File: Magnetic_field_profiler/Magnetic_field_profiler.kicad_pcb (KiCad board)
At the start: 4 copper layers, 130 x 100 mm, 91 parts, among them J1 USB_B_Micro, J2 Conn_01x04_Socket, J3 Conn_01x04_Socket, J4 Screw_Terminal_01x06, Q1 BSS123, SW1 SW_SPDT, U1 STM32F103C8Tx, U10 MLX90393, U11 MLX90393, U12 MLX90393, U13 TP6841S6, U2 MLX90393, U3 DRV8825, U4 DRV8825, U5 MLX90393, U6 MLX90393, U7 MLX90393, U8 MLX90393, U9 MLX90393, Y1 Crystal_GND24

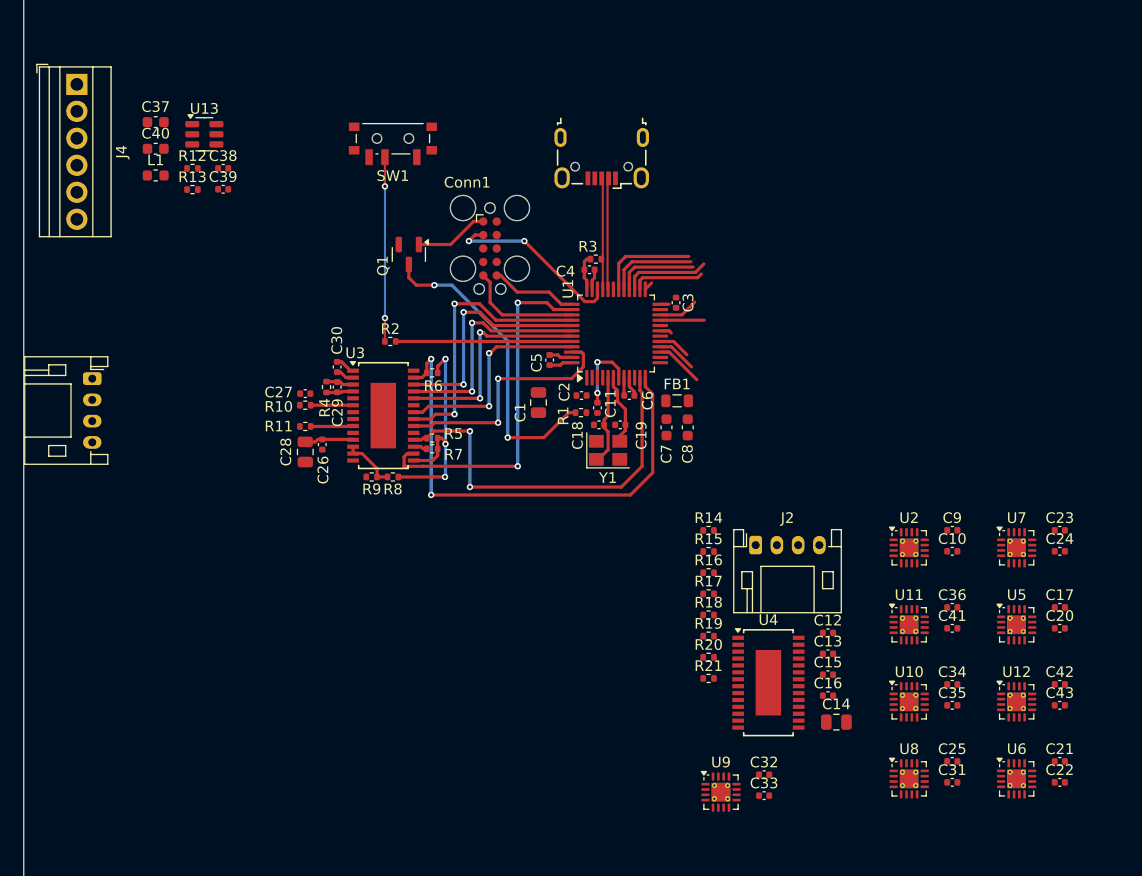
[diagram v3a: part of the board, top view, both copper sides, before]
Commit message: IO expander connections complete and PCB layout restarted
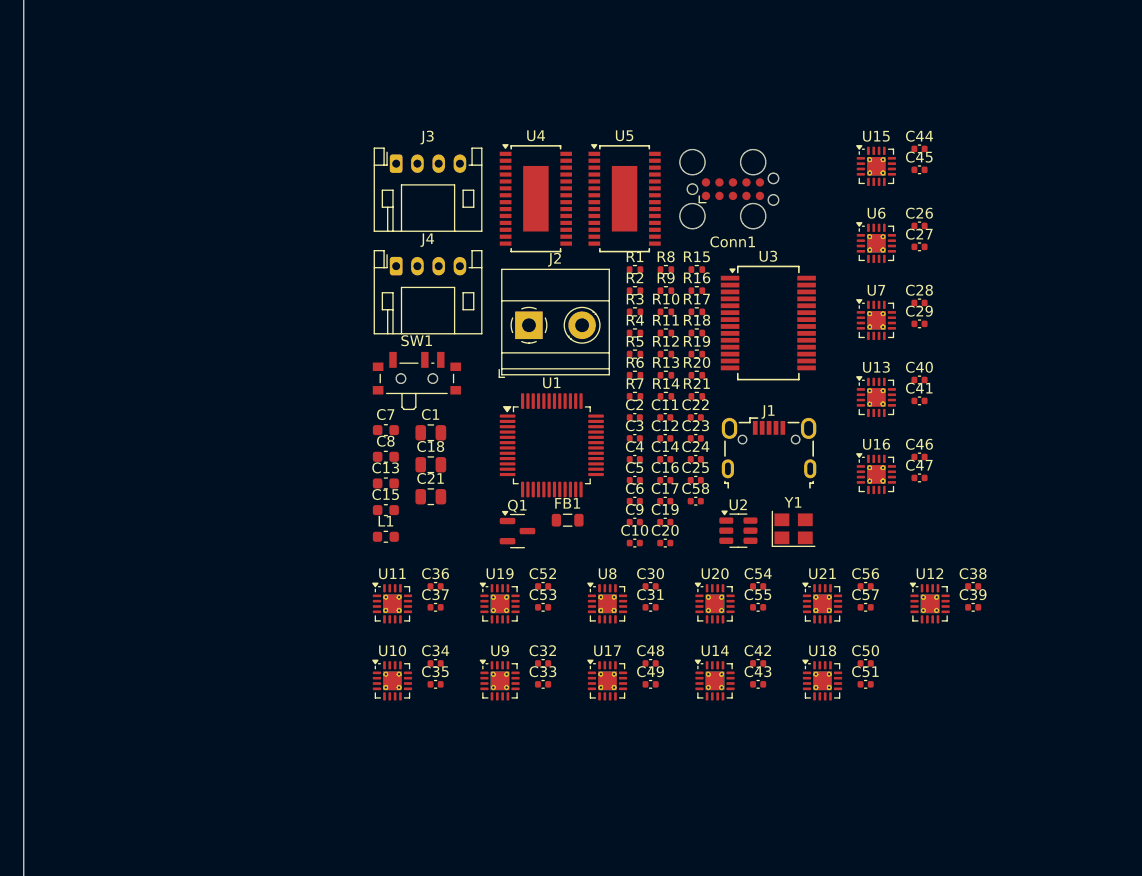
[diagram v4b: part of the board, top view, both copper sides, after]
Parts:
- added C44: 100n, Capacitor_SMD:C_0402_1005Metric, F.Cu at (139.3, 76.4)
- added C45: 100n, Capacitor_SMD:C_0402_1005Metric, F.Cu at (139.3, 78.3)
- added C46: 100n, Capacitor_SMD:C_0402_1005Metric, F.Cu at (139.3, 105.4)
- added C47: 100n, Capacitor_SMD:C_0402_1005Metric, F.Cu at (139.3, 107.3)
- added C48: 100n, Capacitor_SMD:C_0402_1005Metric, F.Cu at (114.0, 124.8)
- added C49: 100n, Capacitor_SMD:C_0402_1005Metric, F.Cu at (114.0, 126.8)
- added C50: 100n, Capacitor_SMD:C_0402_1005Metric, F.Cu at (134.2, 124.8)
- added C51: 100n, Capacitor_SMD:C_0402_1005Metric, F.Cu at (134.2, 126.8)
- added C52: 100n, Capacitor_SMD:C_0402_1005Metric, F.Cu at (103.9, 117.6)
- added C53: 100n, Capacitor_SMD:C_0402_1005Metric, F.Cu at (103.9, 119.5)
- added C54: 100n, Capacitor_SMD:C_0402_1005Metric, F.Cu at (124.1, 117.6)
- added C55: 100n, Capacitor_SMD:C_0402_1005Metric, F.Cu at (124.1, 119.5)
- added C56: 100n, Capacitor_SMD:C_0402_1005Metric, F.Cu at (134.2, 117.6)
- added C57: 100n, Capacitor_SMD:C_0402_1005Metric, F.Cu at (134.2, 119.5)
- added C58: 100n, Capacitor_SMD:C_0402_1005Metric, F.Cu at (118.3, 109.5)
- added U14: MLX90393, Package_DFN_QFN:QFN-16-1EP_3x3mm_P0.5mm_EP1.75x1.75mm_ThermalVias, F.Cu at (120.1, 126.4)
- added U15: MLX90393, Package_DFN_QFN:QFN-16-1EP_3x3mm_P0.5mm_EP1.75x1.75mm_ThermalVias, F.Cu at (135.3, 78.0)
- added U16: MLX90393, Package_DFN_QFN:QFN-16-1EP_3x3mm_P0.5mm_EP1.75x1.75mm_ThermalVias, F.Cu at (135.3, 107.0)
- added U17: MLX90393, Package_DFN_QFN:QFN-16-1EP_3x3mm_P0.5mm_EP1.75x1.75mm_ThermalVias, F.Cu at (109.9, 126.4)
- added U18: MLX90393, Package_DFN_QFN:QFN-16-1EP_3x3mm_P0.5mm_EP1.75x1.75mm_ThermalVias, F.Cu at (130.2, 126.4)
- added U19: MLX90393, Package_DFN_QFN:QFN-16-1EP_3x3mm_P0.5mm_EP1.75x1.75mm_ThermalVias, F.Cu at (99.8, 119.2)
- added U20: MLX90393, Package_DFN_QFN:QFN-16-1EP_3x3mm_P0.5mm_EP1.75x1.75mm_ThermalVias, F.Cu at (120.1, 119.2)
- added U21: MLX90393, Package_DFN_QFN:QFN-16-1EP_3x3mm_P0.5mm_EP1.75x1.75mm_ThermalVias, F.Cu at (130.2, 119.2)
- C10, C11: value 100n -> 10p
- C13, C15: value 100n -> 22u; footprint Capacitor_SMD:C_0402_1005Metric -> Capacitor_SMD:C_0603_1608Metric
- C14, C28: value 100u -> 100n; footprint Capacitor_SMD:C_0805_2012Metric -> Capacitor_SMD:C_0402_1005Metric
- C16, C30: value 10n -> 100n
- C18: value 10p -> 100u; footprint Capacitor_SMD:C_0402_1005Metric -> Capacitor_SMD:C_0805_2012Metric
- C19: value 10p -> 100n
- C21: value 100n -> 100u; footprint Capacitor_SMD:C_0402_1005Metric -> Capacitor_SMD:C_0805_2012Metric
- C24, C25: value 100n -> 10n
- C37, C40: value 22u -> 100n; footprint Capacitor_SMD:C_0603_1608Metric -> Capacitor_SMD:C_0402_1005Metric
- J2: value Conn_01x04_Socket -> Screw_Terminal_01x02; footprint Connector_JST:JST_PH_S4B-PH-K_1x04_P2.00mm_Horizontal -> TerminalBlock_Phoenix:TerminalBlock_Phoenix_MKDS-1,5-2_1x02_P5.00mm_Horizontal
- J4: value Screw_Terminal_01x06 -> Conn_01x04_Socket; footprint TerminalBlock:TerminalBlock_Xinya_XY308-2.54-6P_1x06_P2.54mm_Horizontal -> Connector_JST:JST_PH_S4B-PH-K_1x04_P2.00mm_Horizontal
- R10, R11: value 200m -> 10k
- R12: value 75k -> 10k
- R13: value 24k -> 10k
- R14: value 1M -> 50k
- R15: value 10k -> 50k
- R16, R17: value 10k -> 30k
- R18: value 50k -> 200m
- R19: value 30k -> 200m
- R2: value 10k -> 1k5
- R3: value 1k5 -> 10k
- R4: value 1M -> 75k
- R5: value 10k -> 24k
- R6, R7: value 10k -> 1M
- R8: value 50k -> 10k
- R9: value 30k -> 10k
- U13: value TP6841S6 -> MLX90393; footprint Package_TO_SOT_SMD:SOT-23-6 -> Package_DFN_QFN:QFN-16-1EP_3x3mm_P0.5mm_EP1.75x1.75mm_ThermalVias
- U2: value MLX90393 -> TP6841S6; footprint Package_DFN_QFN:QFN-16-1EP_3x3mm_P0.5mm_EP1.75x1.75mm_ThermalVias -> Package_TO_SOT_SMD:SOT-23-6
- U3: value DRV8825 -> MCP23S17; footprint Package_SO:TSSOP-28-1EP_4.4x9.7mm_P0.65mm -> Package_SO:SSOP-28_5.3x10.2mm_P0.65mm
- U5: value MLX90393 -> DRV8825; footprint Package_DFN_QFN:QFN-16-1EP_3x3mm_P0.5mm_EP1.75x1.75mm_ThermalVias -> Package_SO:TSSOP-28-1EP_4.4x9.7mm_P0.65mm
- moved C38 80.8 mm to (144.4, 117.6)
- moved C39 80.8 mm to (144.4, 119.5)
- moved C40 75.1 mm to (139.3, 98.1)
- moved U13 67.9 mm to (135.3, 99.8)
- moved C21 64.2 mm to (93.3, 109.1)
- moved C26 59.9 mm to (139.3, 83.6), turned to 0 degrees
- moved C28 59.5 mm to (139.3, 90.9), turned to 0 degrees
- moved C27 59.4 mm to (139.3, 85.6), turned to 0 degrees
- moved C29 55.1 mm to (139.3, 92.8), turned to 0 degrees
- moved U5 54.5 mm to (111.6, 81.1)
- moved C37 52.7 mm to (93.8, 119.5)
- moved U6 52.1 mm to (135.3, 85.3)
- moved U4 50.5 mm to (103.2, 81.1)
- moved U11 48.7 mm to (89.7, 119.2)
- moved C34 48.7 mm to (93.8, 124.8)
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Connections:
- C10 pad 1: +3.3V -> /HSE_IN
- C11 pad 1: /NRST -> /HSE_OUT
- C12 pad 1: +12V -> /SMPS_BST
- C12 pad 2: GND -> /SMPS_SW
- C15 pad 1: +12V -> +3.3V
- C15 pad 2: /VCP -> GND
- C16 pad 1: /CP1 -> +12V
- C16 pad 2: /CP2 -> GND
- C17 pad 1: +3.3V -> +12V
- C18 pad 1: /HSE_IN -> +12V
- C19 pad 1: /HSE_OUT -> +12V
- C20 pad 1: +3.3V -> +12V
- C21 pad 1: +3.3V -> +12V
- C22 pad 1: +3.3V -> +12V
- C22 pad 2: GND -> /VCP
- C23 pad 1: +3.3V -> +12V
- C23 pad 2: GND -> /VCP
- C24 pad 1: +3.3V -> /CP1
- C24 pad 2: GND -> /CP2
- C25 pad 1: +3.3V -> /CP1
- C25 pad 2: GND -> /CP2
- C26 pad 1: +12V -> +3.3V
- C27 pad 1: +12V -> +3.3V
- C28 pad 1: +12V -> +3.3V
- C29 pad 1: +12V -> +3.3V
- C29 pad 2: /VCP -> GND
- C30 pad 1: /CP1 -> +3.3V
- C30 pad 2: /CP2 -> GND
- C37 pad 1: +12V -> +3.3V
- C38 pad 1: +12V -> +3.3V
- C39 pad 1: /SMPS_BST -> +3.3V
- C39 pad 2: /SMPS_SW -> GND
- C9 pad 1: +3.3V -> /NRST
- J2 pad 1: /M2_AOUT1 -> GND
- J2 pad 2: /M2_AOUT2 -> +12V
- J4 pad 1: GND -> /M2_AOUT1
- J4 pad 2: GND -> /M2_AOUT2
- J4 pad 3: GND -> /M2_BOUT1
- J4 pad 4: +12V -> /M2_BOUT2
- R1 pad 1: /SWD_D -> /SW_BOOT0
- R1 pad 2: /NRST -> /BOOT0
- R10 pad 1: /ISENA -> /M2_V3P3OUT
- R10 pad 2: GND -> /MTR2_NFAULT
- R11 pad 1: GND -> /M2_V3P3OUT
- R11 pad 2: /ISENB -> /MTR2_NHOME
- R12 pad 1: /SMPS_FB -> /V3P3OUT
- R12 pad 2: +3.3V -> /MTR_NSLEEP
- R13 pad 1: GND -> /V3P3OUT
- R13 pad 2: /SMPS_FB -> /MTR_NSLEEP
- R14 pad 1: +12V -> /V3P3OUT
- R14 pad 2: /VCP -> /AVREF
- R15 pad 1: /M2_V3P3OUT -> /V3P3OUT
- R15 pad 2: /MTR2_NFAULT -> /AVREF
- R16 pad 1: /M2_V3P3OUT -> /AVREF
- R16 pad 2: /MTR2_NHOME -> GND
- R17 pad 1: /V3P3OUT -> /AVREF
- R17 pad 2: /MTR_NSLEEP -> GND
- R18 pad 1: /V3P3OUT -> /ISENA
- R18 pad 2: /AVREF -> GND
- R19 pad 1: /AVREF -> /ISENA
- R2 pad 1: /SW_BOOT0 -> +3.3V
- R2 pad 2: /BOOT0 -> /USB_D+
- R20 pad 1: /ISENA -> GND
- R20 pad 2: GND -> /ISENB
- R3 pad 1: +3.3V -> /SWD_D
- R3 pad 2: /USB_D+ -> /NRST
- R4 pad 1: +12V -> /SMPS_FB
- R4 pad 2: /VCP -> +3.3V
- R5 pad 1: /M1_V3P3OUT -> GND
- R5 pad 2: /MTR1_NFAULT -> /SMPS_FB
- R6 pad 1: /M1_V3P3OUT -> +12V
- R6 pad 2: /MTR1_NHOME -> /VCP
- R7 pad 1: /V3P3OUT -> +12V
- R7 pad 2: /MTR_NSLEEP -> /VCP
- R8 pad 1: /V3P3OUT -> /M1_V3P3OUT
- R8 pad 2: /AVREF -> /MTR1_NFAULT
- R9 pad 1: /AVREF -> /M1_V3P3OUT
- R9 pad 2: GND -> /MTR1_NHOME
- U1 pad 19: /MAG_CS1 -> unconnected-(U1-PB1-Pad19)
- U1 pad 20: /MAG_CS2 -> unconnected-(U1-PB2-Pad20)
- U1 pad 21: /MAG_CS3 -> unconnected-(U1-PB10-Pad21)
- U1 pad 22: /MAG_CS4 -> unconnected-(U1-PB11-Pad22)
- U1 pad 25: /MAG_CS5 -> unconnected-(U1-PB12-Pad25)
- U1 pad 26: /MAG_CS6 -> unconnected-(U1-PB13-Pad26)
- U1 pad 27: /MAG_CS9 -> /IO_RST
- U1 pad 28: /MAG_CS8 -> /IO_CS
- U1 pad 29: /MAG_CS7 -> unconnected-(U1-PA8-Pad29)
- U10 pad 2: /MAG_CS3 -> /MAG_CS5
- U12 pad 2: /MAG_CS9 -> /MAG_CS7
- U13 pad 1: /SMPS_BST -> unconnected-(U13-INT-Pad1)
- U13 pad 2: GND -> /MAG_CS8
- U13 pad 3: /SMPS_FB -> /SPI.SPI_MISO
- U13 pad 4: +12V -> unconnected-(U13-NC-Pad4)
- U13 pad 5: +12V -> /SPI.SPI_CLK
- U13 pad 6: /SMPS_SW -> /SPI.SPI_MOSI
- U2 pad 1: unconnected-(U2-INT-Pad1) -> /SMPS_BST
- U2 pad 2: /MAG_CS1 -> GND
- U2 pad 3: /SPI.SPI_MISO -> /SMPS_FB
- U2 pad 4: unconnected-(U2-NC-Pad4) -> +12V
- U2 pad 5: /SPI.SPI_CLK -> +12V
- U2 pad 6: /SPI.SPI_MOSI -> /SMPS_SW
- U3 pad 1: /CP1 -> /MAG_CS9
- U3 pad 10: /M1_BOUT1 -> GND
- U3 pad 11: +12V -> /IO_CS
- U3 pad 12: /AVREF -> /SPI.SPI_CLK
- U3 pad 13: /AVREF -> /SPI.SPI_MOSI
- U3 pad 14: GND -> /SPI.SPI_MISO
- U3 pad 15: /M1_V3P3OUT -> GND
- U3 pad 16: /MTR_NRST -> GND
- U3 pad 17: /MTR_NSLEEP -> GND
- U3 pad 18: /MTR1_NFAULT -> /IO_RST
- U3 pad 2: /CP2 -> /MAG_CS10
- U3 pad 20: /MTR1_DIR -> unconnected-(U3-INTA-Pad20)
- U3 pad 21: /MTR_NEN -> /MAG_CS1
- U3 pad 22: /MTR1_STEP -> /MAG_CS2
- U3 pad 23: unconnected-(U3-NC-Pad23) -> /MAG_CS3
- U3 pad 24: /MTR_MODE0 -> /MAG_CS4
- U3 pad 25: /MTR_MODE1 -> /MAG_CS5
- U3 pad 26: /MTR_MODE2 -> /MAG_CS6
- U3 pad 27: /MTR1_NHOME -> /MAG_CS7
- U3 pad 28: GND -> /MAG_CS8
- U3 pad 3: /VCP -> /MAG_CS11
- U3 pad 4: +12V -> /MAG_CS12
- U3 pad 5: /M1_AOUT1 -> /MAG_CS13
- U3 pad 6: /ISENA -> /MAG_CS14
- U3 pad 7: /M1_AOUT2 -> /MAG_CS15
- U3 pad 8: /M1_BOUT2 -> /MAG_CS16
- U3 pad 9: /ISENB -> +3.3V
- U4 pad 10: /M2_BOUT1 -> /M1_BOUT1
- U4 pad 15: /M2_V3P3OUT -> /M1_V3P3OUT
- U4 pad 18: /MTR2_NFAULT -> /MTR1_NFAULT
- U4 pad 20: /MTR2_DIR -> /MTR1_DIR
- U4 pad 22: /MTR2_STEP -> /MTR1_STEP
- U4 pad 27: /MTR2_NHOME -> /MTR1_NHOME
- U4 pad 5: /M2_AOUT1 -> /M1_AOUT1
- U4 pad 7: /M2_AOUT2 -> /M1_AOUT2
- U4 pad 8: /M2_BOUT2 -> /M1_BOUT2
- U5 pad 1: unconnected-(U5-INT-Pad1) -> /CP1
- U5 pad 10: unconnected-(U5-NC-Pad10) -> /M2_BOUT1
- U5 pad 11: GND -> +12V
- U5 pad 12: GND -> /AVREF
- U5 pad 13: GND -> /AVREF
- U5 pad 14: unconnected-(U5-NC-Pad14) -> GND
- U5 pad 15: +3.3V -> /M2_V3P3OUT
- U5 pad 16: unconnected-(U5-NC-Pad16) -> /MTR_NRST
- U5 pad 17: GND -> /MTR_NSLEEP
- U5 pad 2: /MAG_CS4 -> /CP2
- U5 pad 3: /SPI.SPI_MISO -> /VCP
- U5 pad 4: unconnected-(U5-NC-Pad4) -> +12V
- U5 pad 5: /SPI.SPI_CLK -> /M2_AOUT1
- U5 pad 6: /SPI.SPI_MOSI -> /ISENA
- U5 pad 7: /MAG_TRIG -> /M2_AOUT2
- U5 pad 8: +3.3V -> /M2_BOUT2
- U5 pad 9: unconnected-(U5-NC-Pad9) -> /ISENB
- U6 pad 2: /MAG_CS7 -> /MAG_CS1
- U8 pad 2: /MAG_CS5 -> /MAG_CS3
- U9 pad 2: /MAG_CS8 -> /MAG_CS4
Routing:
- net /MTR1_NHOME: track 46.6 -> 0.00 mm, vias 2 -> 0
- net /MTR1_NFAULT: track 36.3 -> 0.00 mm, vias 2 -> 0
- net /MTR_NRST: track 33.5 -> 0.00 mm, vias 2 -> 0
- net /SWD_D: track 29.5 -> 0.00 mm, vias 2 -> 0
- net /MTR_NEN: track 26.1 -> 0.00 mm, vias 2 -> 0
- net /MTR1_DIR: track 22.7 -> 0.00 mm, vias 2 -> 0
- net /V3P3OUT: track 22.3 -> 0.00 mm, vias 3 -> 0
- net /MTR_MODE2: track 22.2 -> 0.00 mm, vias 2 -> 0
- net /MTR_MODE1: track 21.7 -> 0.00 mm, vias 2 -> 0
- net /MTR_MODE0: track 21.2 -> 0.00 mm, vias 2 -> 0
- net /MTR1_STEP: track 20.5 -> 0.00 mm, vias 2 -> 0
- net /SW_BOOT0: track 17.5 -> 0.00 mm, vias 2 -> 0
- net /SWDIO: track 17.0 -> 0.00 mm, vias 2 -> 0
- net /BOOT0: track 16.5 -> 0.00 mm
- net /USB_D-: track 11.1 -> 0.00 mm
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
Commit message: Swapping MCU IOs and defining netclasses
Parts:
- removed C26, C27, C28, C29, C30, C31, C32, C33, C34, C35, C36, C37, C38, C39, C40, C41, C42, C43, C44, C45, C46, C47, C48, C49, C50, C51, C52, C53, C54, C55, C56, C57: 100n, Capacitor_SMD:C_0402_1005Metric
- removed U10, U11, U12, U13, U14, U15, U16, U17, U18, U19, U20, U21, U6, U7, U8, U9: MLX90393, Package_DFN_QFN:QFN-16-1EP_3x3mm_P0.5mm_EP1.75x1.75mm_ThermalVias

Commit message: Initial PCB layout
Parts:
- added C26: 470n, Capacitor_SMD:C_0402_1005Metric, F.Cu at (137.8, 75.7)
- added C27: 470n, Capacitor_SMD:C_0402_1005Metric, F.Cu at (137.8, 77.6)
- added C28: 10n, Capacitor_SMD:C_0201_0603Metric, F.Cu at (137.6, 79.5)
- added C29: 10n, Capacitor_SMD:C_0201_0603Metric, F.Cu at (137.6, 81.2)
- added C30: 100n, Capacitor_SMD:C_0201_0603Metric, F.Cu at (157.5, 75.5)
- added C31: 100n, Capacitor_SMD:C_0201_0603Metric, F.Cu at (157.5, 77.3)
- added C32: 100n, Capacitor_SMD:C_0201_0603Metric, F.Cu at (167.2, 75.5)
- added C33: 100n, Capacitor_SMD:C_0201_0603Metric, F.Cu at (167.2, 77.3)
- added C34: 100n, Capacitor_SMD:C_0201_0603Metric, F.Cu at (157.5, 90.0)
- added C35: 100n, Capacitor_SMD:C_0201_0603Metric, F.Cu at (157.5, 91.8)
- added C36: 100n, Capacitor_SMD:C_0201_0603Metric, F.Cu at (147.8, 104.5)
- added C37: 100n, Capacitor_SMD:C_0201_0603Metric, F.Cu at (147.8, 106.3)
- added C38: 100n, Capacitor_SMD:C_0201_0603Metric, F.Cu at (147.8, 90.0)
- added C39: 100n, Capacitor_SMD:C_0201_0603Metric, F.Cu at (147.8, 91.8)
- added C40: 100n, Capacitor_SMD:C_0201_0603Metric, F.Cu at (167.2, 82.8)
- added C41: 100n, Capacitor_SMD:C_0201_0603Metric, F.Cu at (167.2, 84.5)
- added C42: 100n, Capacitor_SMD:C_0201_0603Metric, F.Cu at (167.2, 104.5)
- added C43: 100n, Capacitor_SMD:C_0201_0603Metric, F.Cu at (167.2, 106.3)
- added C44: 100n, Capacitor_SMD:C_0201_0603Metric, F.Cu at (147.8, 82.8)
- added C45: 100n, Capacitor_SMD:C_0201_0603Metric, F.Cu at (147.8, 84.5)
- added C46: 100n, Capacitor_SMD:C_0201_0603Metric, F.Cu at (157.5, 97.3)
- added C47: 100n, Capacitor_SMD:C_0201_0603Metric, F.Cu at (157.5, 99.0)
- added C48: 100n, Capacitor_SMD:C_0201_0603Metric, F.Cu at (147.8, 75.5)
- added C49: 100n, Capacitor_SMD:C_0201_0603Metric, F.Cu at (147.8, 77.3)
- added C50: 100n, Capacitor_SMD:C_0201_0603Metric, F.Cu at (157.5, 82.8)
- added C51: 100n, Capacitor_SMD:C_0201_0603Metric, F.Cu at (157.5, 84.5)
- added C52: 100n, Capacitor_SMD:C_0201_0603Metric, F.Cu at (167.2, 90.0)
- added C53: 100n, Capacitor_SMD:C_0201_0603Metric, F.Cu at (167.2, 91.8)
- added C54: 100n, Capacitor_SMD:C_0201_0603Metric, F.Cu at (167.2, 97.3)
- added C55: 100n, Capacitor_SMD:C_0201_0603Metric, F.Cu at (167.2, 99.0)
- added C56: 100n, Capacitor_SMD:C_0201_0603Metric, F.Cu at (147.8, 97.3)
- added C57: 100n, Capacitor_SMD:C_0201_0603Metric, F.Cu at (147.8, 99.0)
- added C59: 100n, Capacitor_SMD:C_0201_0603Metric, F.Cu at (133.2, 90.2)
- added C60: 100n, Capacitor_SMD:C_0201_0603Metric, F.Cu at (157.5, 104.5)
- added C61: 100n, Capacitor_SMD:C_0201_0603Metric, F.Cu at (157.5, 106.3)
- added D1: STATUS_LED, LED_SMD:LED_0805_2012Metric, F.Cu at (134.2, 76.2)
- added D2: PWR_LED, LED_SMD:LED_0805_2012Metric, F.Cu at (134.2, 79.2)
- added U10: MLX90393, Package_DFN_QFN:QFN-16-1EP_3x3mm_P0.5mm_EP1.75x1.75mm_ThermalVias, F.Cu at (143.9, 91.8)
- added U11: MLX90393, Package_DFN_QFN:QFN-16-1EP_3x3mm_P0.5mm_EP1.75x1.75mm_ThermalVias, F.Cu at (163.3, 84.5)
- added U12: MLX90393, Package_DFN_QFN:QFN-16-1EP_3x3mm_P0.5mm_EP1.75x1.75mm_ThermalVias, F.Cu at (163.3, 106.3)
- added U13: MLX90393, Package_DFN_QFN:QFN-16-1EP_3x3mm_P0.5mm_EP1.75x1.75mm_ThermalVias, F.Cu at (143.9, 84.5)
- added U14: MLX90393, Package_DFN_QFN:QFN-16-1EP_3x3mm_P0.5mm_EP1.75x1.75mm_ThermalVias, F.Cu at (153.6, 99.0)
- added U15: MLX90393, Package_DFN_QFN:QFN-16-1EP_3x3mm_P0.5mm_EP1.75x1.75mm_ThermalVias, F.Cu at (143.9, 77.3)
- added U16: MLX90393, Package_DFN_QFN:QFN-16-1EP_3x3mm_P0.5mm_EP1.75x1.75mm_ThermalVias, F.Cu at (153.6, 84.5)
- added U17: MLX90393, Package_DFN_QFN:QFN-16-1EP_3x3mm_P0.5mm_EP1.75x1.75mm_ThermalVias, F.Cu at (163.3, 91.8)
- added U18: MLX90393, Package_DFN_QFN:QFN-16-1EP_3x3mm_P0.5mm_EP1.75x1.75mm_ThermalVias, F.Cu at (163.3, 99.0)
- added U19: MLX90393, Package_DFN_QFN:QFN-16-1EP_3x3mm_P0.5mm_EP1.75x1.75mm_ThermalVias, F.Cu at (143.9, 99.0)
- added U20: MLX90393, Package_DFN_QFN:QFN-16-1EP_3x3mm_P0.5mm_EP1.75x1.75mm_ThermalVias, F.Cu at (134.6, 86.7)
- added U21: MLX90393, Package_DFN_QFN:QFN-16-1EP_3x3mm_P0.5mm_EP1.75x1.75mm_ThermalVias, F.Cu at (153.6, 106.3)
- added U6: MLX90393, Package_DFN_QFN:QFN-16-1EP_3x3mm_P0.5mm_EP1.75x1.75mm_ThermalVias, F.Cu at (153.6, 77.3)
- added U7: MLX90393, Package_DFN_QFN:QFN-16-1EP_3x3mm_P0.5mm_EP1.75x1.75mm_ThermalVias, F.Cu at (163.3, 77.3)
- added U8: MLX90393, Package_DFN_QFN:QFN-16-1EP_3x3mm_P0.5mm_EP1.75x1.75mm_ThermalVias, F.Cu at (153.6, 91.8)
- added U9: MLX90393, Package_DFN_QFN:QFN-16-1EP_3x3mm_P0.5mm_EP1.75x1.75mm_ThermalVias, F.Cu at (143.9, 106.3)
- C1: footprint Capacitor_SMD:C_0805_2012Metric -> Capacitor_THT:CP_Radial_D5.0mm_P2.00mm
- C12, C19, C2, C22, C3, C4, C5, C58, C6, C9: footprint Capacitor_SMD:C_0402_1005Metric -> Capacitor_SMD:C_0201_0603Metric
- C13, C15: value 22u -> 100n; footprint Capacitor_SMD:C_0603_1608Metric -> Capacitor_SMD:C_0201_0603Metric
- C14, C16, C17: value 100n -> 22u; footprint Capacitor_SMD:C_0402_1005Metric -> Capacitor_SMD:C_1206_3216Metric
- C18, C21: value 100u -> 100n; footprint Capacitor_SMD:C_0805_2012Metric -> Capacitor_SMD:C_0201_0603Metric
- C20, C23: value 100n -> 100u; footprint Capacitor_SMD:C_0402_1005Metric -> Capacitor_THT:CP_Radial_D5.0mm_P2.00mm
- C24, C25: value 10n -> 100n; footprint Capacitor_SMD:C_0402_1005Metric -> Capacitor_SMD:C_0201_0603Metric
- L1: value 100u -> 3u9; footprint Inductor_SMD:L_0603_1608Metric -> Inductor_SMD:L_Abracon_ASPI-3012S
- R1, R10, R11, R12, R13, R8, R9: footprint Resistor_SMD:R_0402_1005Metric -> Resistor_SMD:R_0805_2012Metric
- R18, R19, R20, R21: footprint Resistor_SMD:R_0402_1005Metric -> Resistor_SMD:R_1206_3216Metric
- R3: value 10k -> 1k
- R4: value 75k -> 10k; footprint Resistor_SMD:R_0402_1005Metric -> Resistor_SMD:R_0805_2012Metric
- R5: value 24k -> 1k
- U2: value TP6841S6 -> AP63203WU; footprint Package_TO_SOT_SMD:SOT-23-6 -> Package_TO_SOT_SMD:TSOT-23-6
- moved J1 80.5 mm to (55.0, 65.0), turned to -90 degrees
- moved U2 51.6 mm to (70.8, 116.3)
- moved J2 51.2 mm to (55.5, 113.2), turned to -90 degrees
- moved SW1 49.9 mm to (52.2, 127.8), turned to -90 degrees
- moved U5 46.1 mm to (70.2, 101.3)
- moved R1 36.5 mm to (137.3, 114.5)
- moved R10 36.5 mm to (140.2, 118.5)
- moved R11 36.5 mm to (140.2, 120.5)
- moved R12 36.5 mm to (140.2, 122.4)
- moved R13 36.5 mm to (140.2, 124.4)
- moved R4 36.5 mm to (137.3, 120.5)
- moved R8 36.5 mm to (140.2, 114.5)
- moved R9 36.5 mm to (140.2, 116.5)
- moved J4 34.9 mm to (56.9, 98.3), turned to -90 degrees
- moved J3 33.3 mm to (56.9, 75.0), turned to -90 degrees
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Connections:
- C12 pad 1: /SMPS_BST -> +3.3V
- C12 pad 2: /SMPS_SW -> GND
- C13 pad 1: +12V -> /SMPS_BST
- C13 pad 2: GND -> /SMPS_SW
- C14 pad 1: +12V -> GND
- C14 pad 2: GND -> +12V
- C15 pad 1: +3.3V -> +12V
- C16 pad 1: +12V -> +3.3V
- C17 pad 1: +12V -> +3.3V
- C22 pad 2: /VCP -> GND
- C23 pad 2: /VCP -> GND
- C24 pad 1: /CP1 -> +12V
- C24 pad 2: /CP2 -> /VCP1
- C25 pad 1: /CP1 -> +12V
- C25 pad 2: /CP2 -> /VCP2
- R12 pad 1: /V3P3OUT -> /M1_V3P3OUT
- R13 pad 1: /V3P3OUT -> /M2_V3P3OUT
- R14 pad 1: /V3P3OUT -> /M1_V3P3OUT
- R14 pad 2: /AVREF -> /REF1
- R15 pad 1: /V3P3OUT -> /M2_V3P3OUT
- R15 pad 2: /AVREF -> /REF2
- R16 pad 1: /AVREF -> /REF1
- R17 pad 1: /AVREF -> /REF2
- R3 pad 1: /SWD_D -> GND
- R3 pad 2: /NRST -> Net-(D1-K)
- R4 pad 1: /SMPS_FB -> /SWD_D
- R4 pad 2: +3.3V -> /NRST
- R5 pad 2: /SMPS_FB -> Net-(D2-K)
- R6 pad 2: /VCP -> /VCP1
- R7 pad 2: /VCP -> /VCP2
- U1 pad 25: unconnected-(U1-PB12-Pad25) -> /IO_CS
- U1 pad 26: unconnected-(U1-PB13-Pad26) -> /IO_RST
- U1 pad 27: /IO_RST -> /MAG_TRIG
- U1 pad 28: /IO_CS -> Net-(D1-A)
- U1 pad 30: /MAG_TRIG -> unconnected-(U1-PA9-Pad30)
- U2 pad 1: /SMPS_BST -> +3.3V
- U2 pad 2: GND -> +12V
- U2 pad 3: /SMPS_FB -> +12V
- U2 pad 4: +12V -> GND
- U2 pad 5: +12V -> /SMPS_SW
- U2 pad 6: /SMPS_SW -> /SMPS_BST
- U4 pad 12: /AVREF -> /REF1
- U4 pad 13: /AVREF -> /REF1
- U4 pad 3: /VCP -> /VCP1
- U5 pad 12: /AVREF -> /REF2
- U5 pad 13: /AVREF -> /REF2
- U5 pad 3: /VCP -> /VCP2
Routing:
- removed copper zone on In1.Cu, net GND
- removed copper zone on In2.Cu, net GND
